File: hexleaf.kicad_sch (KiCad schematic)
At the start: 29 parts

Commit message: added TODO
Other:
- note added: "TODO: - antenna parts - button footprints - gpio setup (led, half-duplex uart)"
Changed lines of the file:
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@@
+    (effects (font (size 1.27 1.27)) (justify left bottom))
+  )
+  (text "TODO:\n\n- antenna parts\n- button footprints\n- gpio setup (led, half-duplex uart)"
+    (at 204.47 130.81 0)
     (effects (font (size 1.27 1.27)) (justify left bottom))
   )

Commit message: added spring connectors & started setup for edge-system
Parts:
- added J?: 009155004201006, 009155004201006, symbol hexleaf:009155004201006
- added PS?: 009155004402006, 009155004402006, symbol hexleaf:009155004402006
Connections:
- net GND: now also PS?.4
- new net: J?.3, PS?.6
- new net EDGE0: J?.4, PS?.3, PS?.5
- new net UART_HALF_DUPLEX: J?.2, PS?.2, PS?.7
- new net VIN: J?.1, PS?.1, PS?.8
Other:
- note added: "Resources: https://www.espressif.com/sites/default/files/documentation/esp32-c3_hardware_design_guidelines_en.pdf"
- note added: "Spring Connectors"
- note added: "TODO: - antenna parts - button footprints - gpio setup (led, half-duplex uart) - edge-system and connections"
- note removed: "TODO: - antenna parts - button footprints - gpio setup (led, half-duplex uart)"
- note removed: "https://www.espressif.com/sites/default/files/documentation/esp32-c3_hardware_design_guidelines_en.pdf"
- moved on the sheet: ANT?, C?, J?, L?, R?, SW?, Y?

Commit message: antenna parts
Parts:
- removed ANT?: 2450AT14A0100T, ANTC1608X40N, symbol hexleaf:2450AT14A0100T
- removed C? (x2): C_Small, symbol Device:C_Small
- removed L?: L_Small, symbol Device:L_Small
- added ANT1: AMCA31-2R450G-S1F-T3, hexleaf:ANTC3216X140N, symbol hexleaf:AMCA31-2R450G-S1F-T3
- added C8: 5p, Capacitor_SMD:C_0603_1608Metric, symbol Device:C_Small
- added L2: 1.8n, Inductor_SMD:L_0603_1608Metric, symbol Device:L_Small
- C6: renamed from C?; value C_Small -> 4p; footprint (none) -> Capacitor_SMD:C_0603_1608Metric; MFN (none) -> 81-GQM1875C2E4R0WB2D
- IC1: renamed from IC?; footprint QFN50P500X500X90-33N-D -> hexleaf:QFN50P500X500X90-33N-D
- J1: renamed from J?; footprint 009155004201006 -> hexleaf:009155004201006
- J2: renamed from J?; footprint (none) -> Connector_PinHeader_2.54mm:PinHeader_1x04_P2.54mm_Vertical
- L1: renamed from L?; value L_Small -> 2n; footprint (none) -> Capacitor_SMD:C_0402_1005Metric; MFN (none) -> 81-LQG15HZ2N0C02D
- PS1: renamed from PS?; footprint 009155004402006 -> hexleaf:009155004402006
- SW1, SW2: renamed from SW?; footprint (none) -> hexleaf:KXT3-1831561
- Y1: renamed from Y?; footprint ECS4001037B2CKMTR -> hexleaf:ECS4001037B2CKMTR
- gave numbers to parts that had none: 18
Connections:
- net ESP_EN: now also IC1.7 (CHIP_EN)
- net GND: now also C8.2
- net LNA_IN: now also C8.1, L2.2
- net at C6.1: now also ANT1.1 (FEED), L2.1
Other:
- note added: "50Ω Feed Line"
- note added: "Resources: https://www.espressif.com/sites/default/files/documentation/esp32-c3_hardware_design_guidelines_en.pdf Antenna: https://electronics.stackexchange.com/questions/598852/impedance-matching-for-esp32-d0wd-v3-qfn-5x5-connected-to-ufl-port https://www.eeweb.com/tools/pi-match/"
- note added: "TODO: - gpio setup (led, half-duplex uart) - edge-system and connections"
- note added: "π-network impedance matching esp: 35Ω + 10j, ant: 50Ω place close to RF output"
- note removed: "Resources: https://www.espressif.com/sites/default/files/documentation/esp32-c3_hardware_design_guidelines_en.pdf"
- note removed: "TODO: - antenna parts - button footprints - gpio setup (led, half-duplex uart) - edge-system and connections"
- moved on the sheet: C12, C6, IC1, R1

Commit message: updated todo
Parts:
- added JP? (x5): SolderJumper_2_Open, Jumper:SolderJumper-2_P1.3mm_Open_TrianglePad1.0x1.5mm, symbol Jumper:SolderJumper_2_Open
- IC1: Manufacturer_Part_Number ESP32-C3 -> ESP32-C3FH4; Mouser Part Number 356-ESP32-C3 -> 356-ESP32-C3FH4; Mouser Price/Stock https://www.mouser.co.uk/ProductDetail/Espressif-Systems/ES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 -> https://www.mouser.de/ProductDetail/Espressif-Systems/ESP32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
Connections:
- net EDGE0: now also IC1.4 (XTAL_32K_P), JP?.1 (A), JP?.1 (A), JP?.1 (A), JP?.1 (A), JP?.1 (A)
- net EDGE1: now also IC1.5 (XTAL_32K_N), JP?.2 (B)
- net EDGE2: now also IC1.14 (GPIO8), JP?.2 (B)
- net EDGE3: now also IC1.16 (GPIO10), JP?.2 (B)
- net EDGE4: now also IC1.19 (SPIHD), JP?.2 (B)
- net EDGE5: now also IC1.26 (GPIO19), JP?.2 (B)
- net UART_HALF_DUPLEX renamed UART_TXRX
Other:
- note added: "TODO: - 12 V -> 3v3 - supply via LED strip (VIN, GND) -> custom footprint for pads - switch to RS485? - fpc connectors for edge signals - gpio setup (led, half-duplex uart)"
- note added: "π-network impedance matching esp: 35Ω + 10i, ant: 50Ω place close to RF output"
- note removed: "TODO: - gpio setup (led, half-duplex uart) - edge-system and connections"
- note removed: "π-network impedance matching esp: 35Ω + 10j, ant: 50Ω place close to RF output"

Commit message: added connectors
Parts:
- added J3, J4: Conn_01x06, hexleaf:fpc_6Pin_0.5mm_ebay, symbol Connector_Generic:Conn_01x06
- added J?: Conn_01x04, symbol Connector_Generic:Conn_01x04
- gave numbers to parts that had none: 5
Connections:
- net EDGE1: now also J3.1 (Pin_1), J4.1 (Pin_1)
- net EDGE2: now also J3.2 (Pin_2), J4.2 (Pin_2)
- net EDGE3: now also J3.3 (Pin_3), J4.3 (Pin_3)
- net EDGE4: now also J3.4 (Pin_4), J4.4 (Pin_4)
- net EDGE5: now also J3.5 (Pin_5), J4.5 (Pin_5)
- net GND: now also J?.4 (Pin_4)
- net VIN: now also J?.1 (Pin_1)
- new net LED_BI: J?.2 (Pin_2)
- new net LED_DI: J?.3 (Pin_3)
- no-connect marks 1 -> 3
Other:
- note added: "Board to strip connector"
- note added: "Connectors"
- note added: "EDGE Jumpers"
- note added: "FPC for EDGE signals"
- note added: "TODO: - 12 V -> 3v3 - switch to RS485? - gpio setup (led, half-duplex uart)"
- note removed: "TODO: - 12 V -> 3v3 - supply via LED strip (VIN, GND) -> custom footprint for pads - switch to RS485? - fpc connectors for edge signals - gpio setup (led, half-duplex uart)"
- moved on the sheet: ANT1, C1, C10, C11, C12, C2, C3, C4, C5, C6, C7, C8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

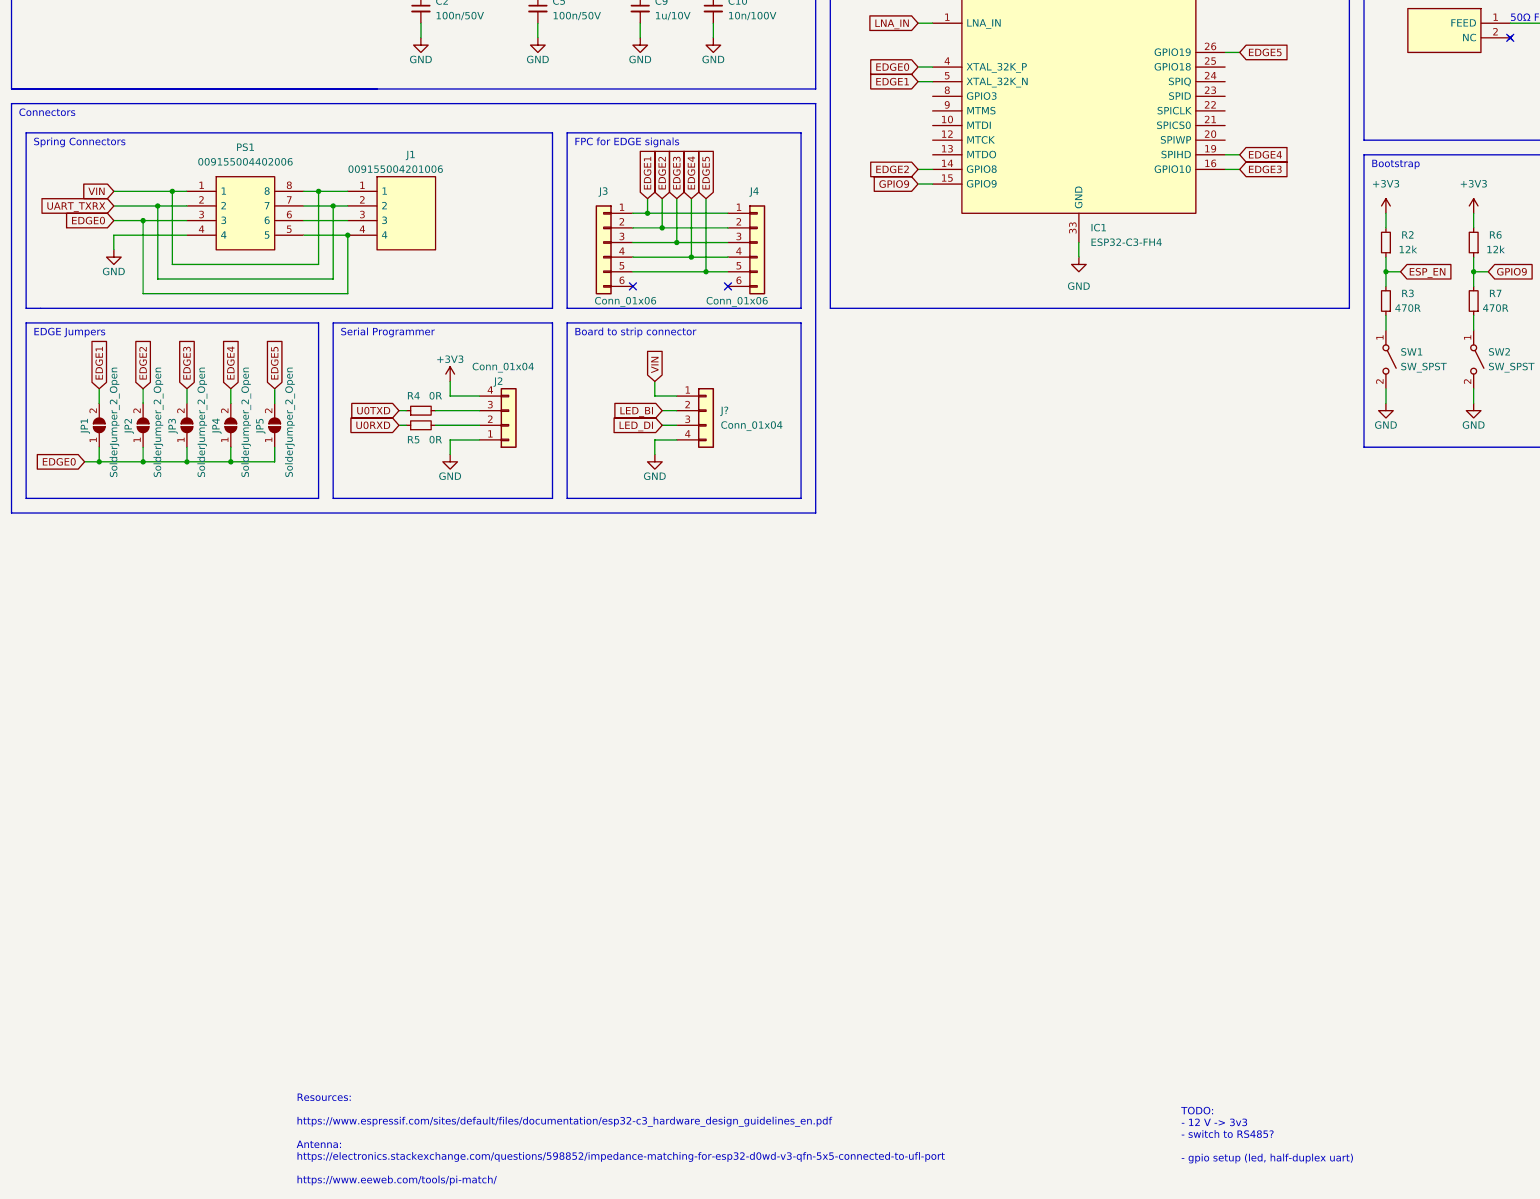
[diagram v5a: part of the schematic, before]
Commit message: added 5 pin connector
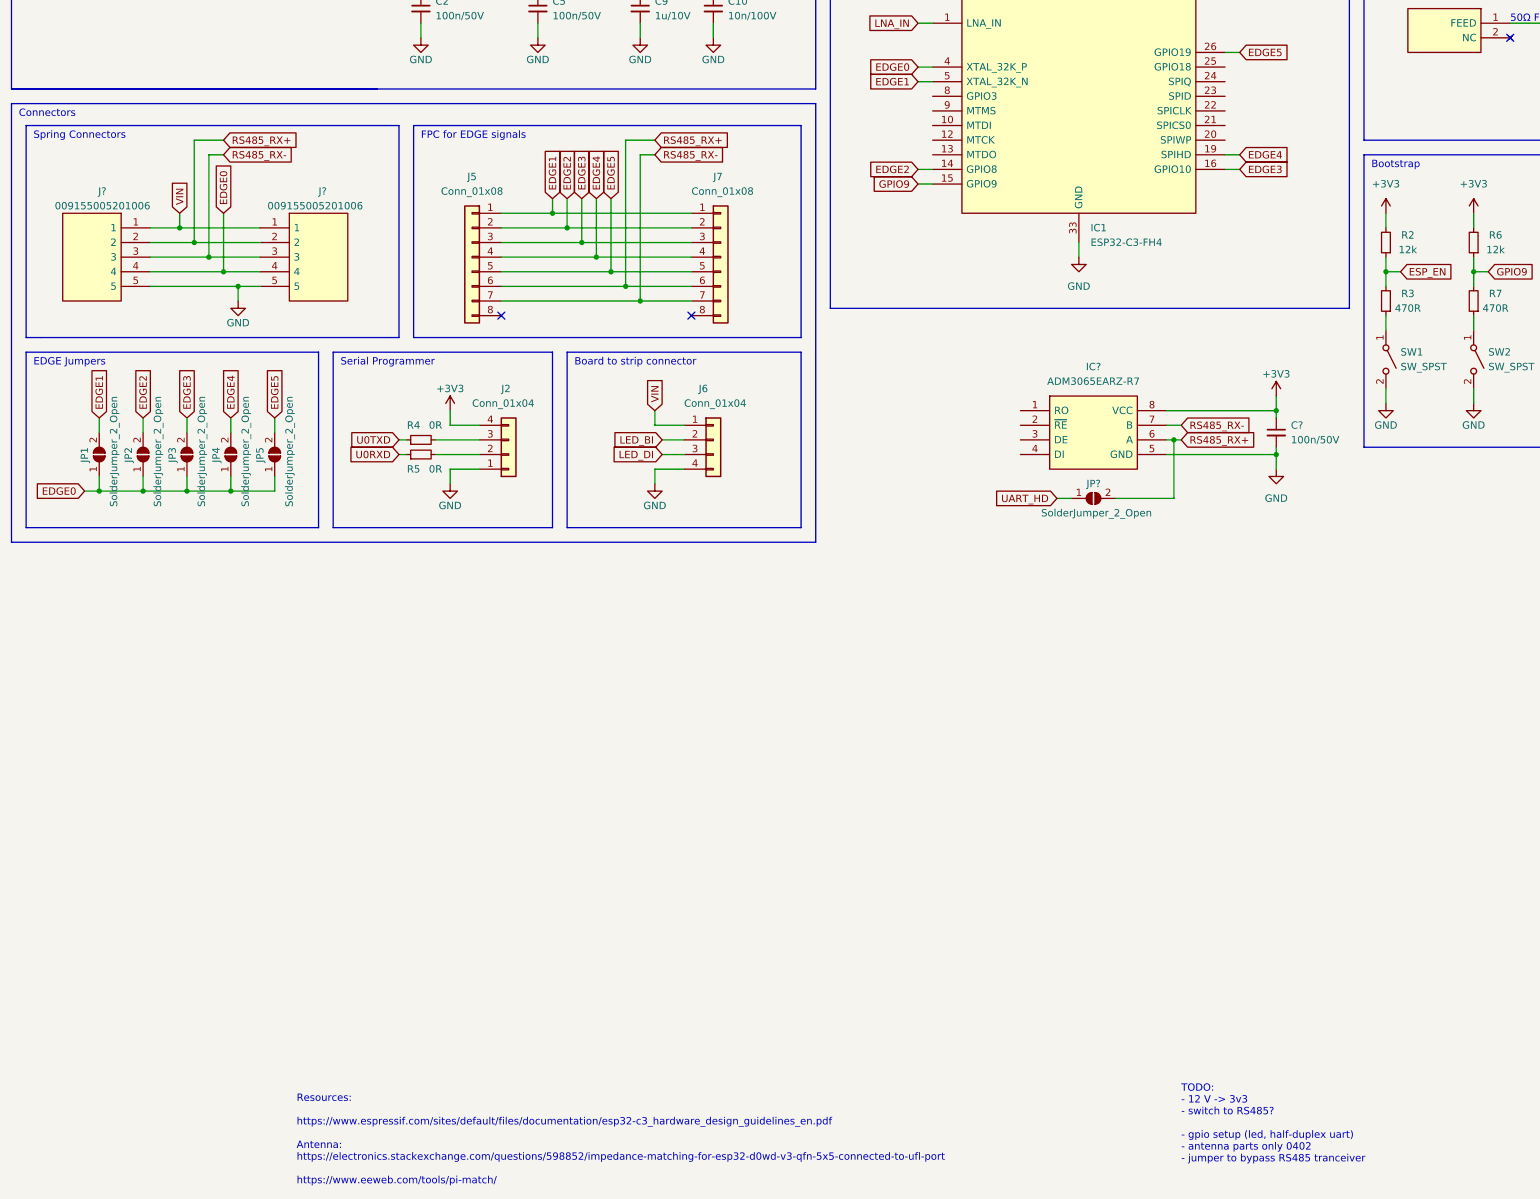
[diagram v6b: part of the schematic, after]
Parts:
- removed J1: 009155004201006, hexleaf:009155004201006, symbol hexleaf:009155004201006
- removed J3, J4: Conn_01x06, hexleaf:fpc_6Pin_0.5mm_ebay, symbol Connector_Generic:Conn_01x06
- removed PS1: 009155004402006, hexleaf:009155004402006, symbol hexleaf:009155004402006
- added C?: 100n/50V, Resistor_SMD:R_0603_1608Metric, symbol Device:C_Small
- added IC?: ADM3065EARZ-R7, SOIC127P600X175-8N, symbol hexleaf:ADM3065EARZ-R7
- added J5, J7: Conn_01x08, symbol Connector_Generic:Conn_01x08
- added J? (x2): 009155005201006, hexleaf:009155005201006, symbol hexleaf:009155005201006
- added JP?: SolderJumper_2_Open, Jumper:SolderJumper-2_P1.3mm_Open_TrianglePad1.0x1.5mm, symbol Jumper:SolderJumper_2_Open
- gave numbers to parts that had none: 1
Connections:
- net +3V3: now also C?.1, IC?.8 (VCC)
- net EDGE0: now also J?.4, J?.4
- net EDGE1: now also J5.1 (Pin_1), J7.1 (Pin_1)
- net EDGE2: now also J5.2 (Pin_2), J7.2 (Pin_2)
- net EDGE3: now also J5.3 (Pin_3), J7.3 (Pin_3)
- net EDGE4: now also J5.4 (Pin_4), J7.4 (Pin_4)
- net EDGE5: now also J5.5 (Pin_5), J7.5 (Pin_5)
- net GND: now also C?.2, IC?.5 (GND), J?.5, J?.5
- net VIN: now also J?.1, J?.1
- new net RS485_RX+: IC?.6 (A), J5.6 (Pin_6), J7.6 (Pin_6), J?.2, J?.2, JP?.2 (B)
- new net RS485_RX-: IC?.7 (B), J5.7 (Pin_7), J7.7 (Pin_7), J?.3, J?.3
- new net UART_HD: JP?.1 (A)
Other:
- note added: "TODO: - 12 V -> 3v3 - switch to RS485? - gpio setup (led, half-duplex uart) - antenna parts only 0402 - jumper to bypass RS485 tranceiver"
- note removed: "TODO: - 12 V -> 3v3 - switch to RS485? - gpio setup (led, half-duplex uart)"
- moved on the sheet: J2, J6, JP1, JP2, JP3, JP4, JP5, R4, R5

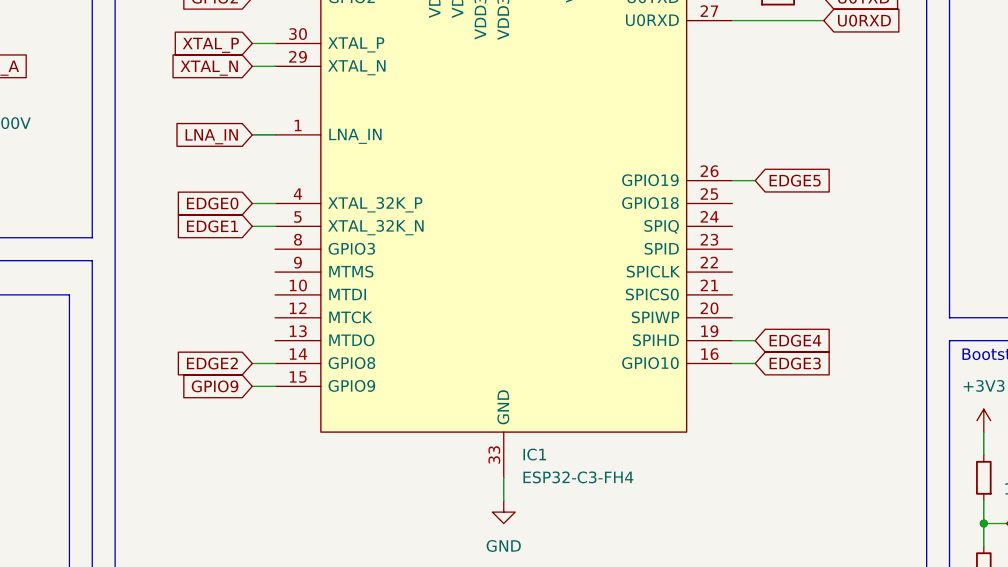
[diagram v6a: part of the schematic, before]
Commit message: moved EDGE signal from GPIO8(strapping pin)
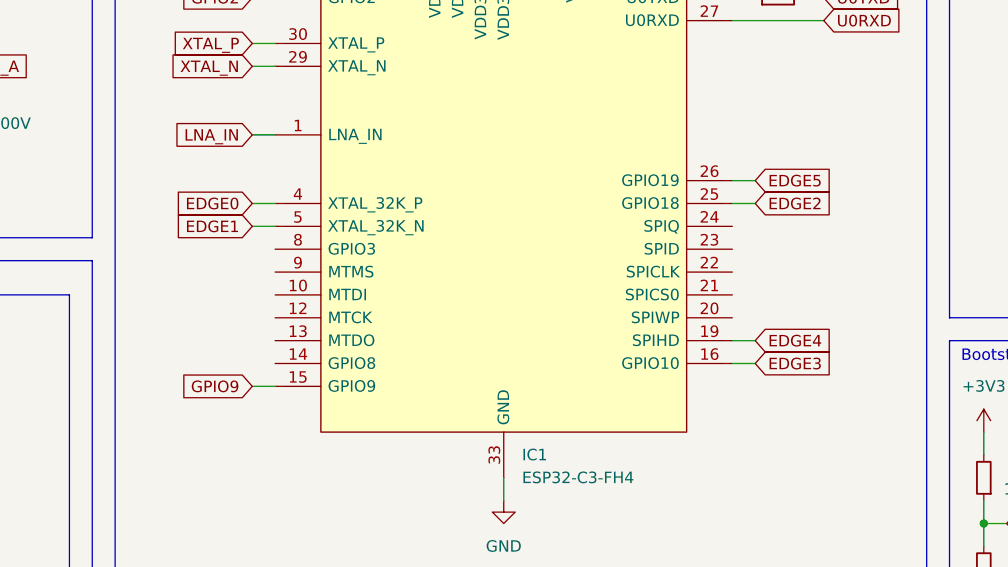
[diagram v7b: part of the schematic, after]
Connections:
- net EDGE2: now also IC1.25 (GPIO18); no longer IC1.14 (GPIO8)
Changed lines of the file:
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@@
     (stroke (width 0) (type default) (color 0 0 0 0))
   )
-  (wire (pts (xy 182.88 102.87) (xy 185.42 102.87))
+  (wire (pts (xy 238.76 85.09) (xy 236.22 85.09))
     (stroke (width 0) (type default) (color 0 0 0 0))
   )
@@
     )
   )
-  (global_label "EDGE2" (shape input) (at 182.88 102.87 180) (fields_autoplaced)
-    (effects (font (size 1.27 1.27)) (justify right))
-    (property "Intersheet References" "${INTERSHEET_REFS}" (id 0) (at 174.5082 102.7906 0)
-      (effects (font (size 1.27 1.27)) (justify right) hide)
-    )
-  )
+  (global_label "EDGE2" (shape input) (at 238.76 85.09 0) (fields_autoplaced)
+    (effects (font (size 1.27 1.27)) (justify left))
+    (property "Intersheet References" "${INTERSHEET_REFS}" (id 0) (at 247.1318 85.1694 0)
+      (effects (font (size 1.27 1.27)) (justify left) hide)
+    )
+  )
